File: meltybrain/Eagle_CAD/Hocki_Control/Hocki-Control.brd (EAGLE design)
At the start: 90 x 46 mm, 113 parts, among them J1 SM03B-SRSS-TB(LF)(SN), J2 SM03B-SRSS-TB(LF)(SN), U1 TEENSY_4.1, U10 TLV3502AIDCNR, U11 NL27WZ32USG, U12 NL27WZ32USG, U13 HMC1052L-TR, U14 LMV358, U15 IRF7509, U16 TMUX1219DCKR, U17 LMV358, U18 LMV358, U19 AP2210K-3.3TRG1, U2 ADXL375, U20 AP2210K-5.0TRG1, U21 MAX20075ATCA/V+, U3 ADXL375, U4 ADXL375, U5 ADXL375, U6 LMH6612MAX/NOPB, U7 LMH6612MAX/NOPB, U8 LMH6612MAX/NOPB, U9 LMH6612MAX/NOPB

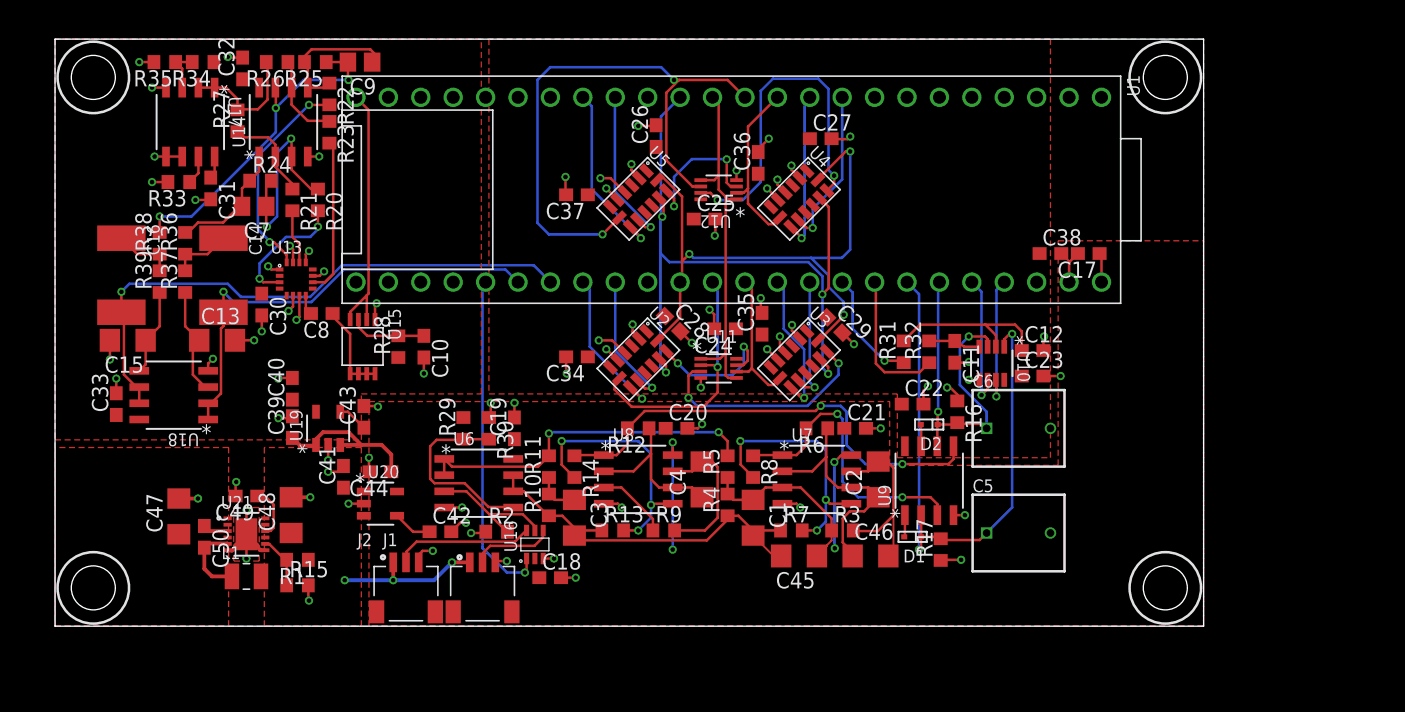
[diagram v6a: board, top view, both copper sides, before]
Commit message: errr---added a connector
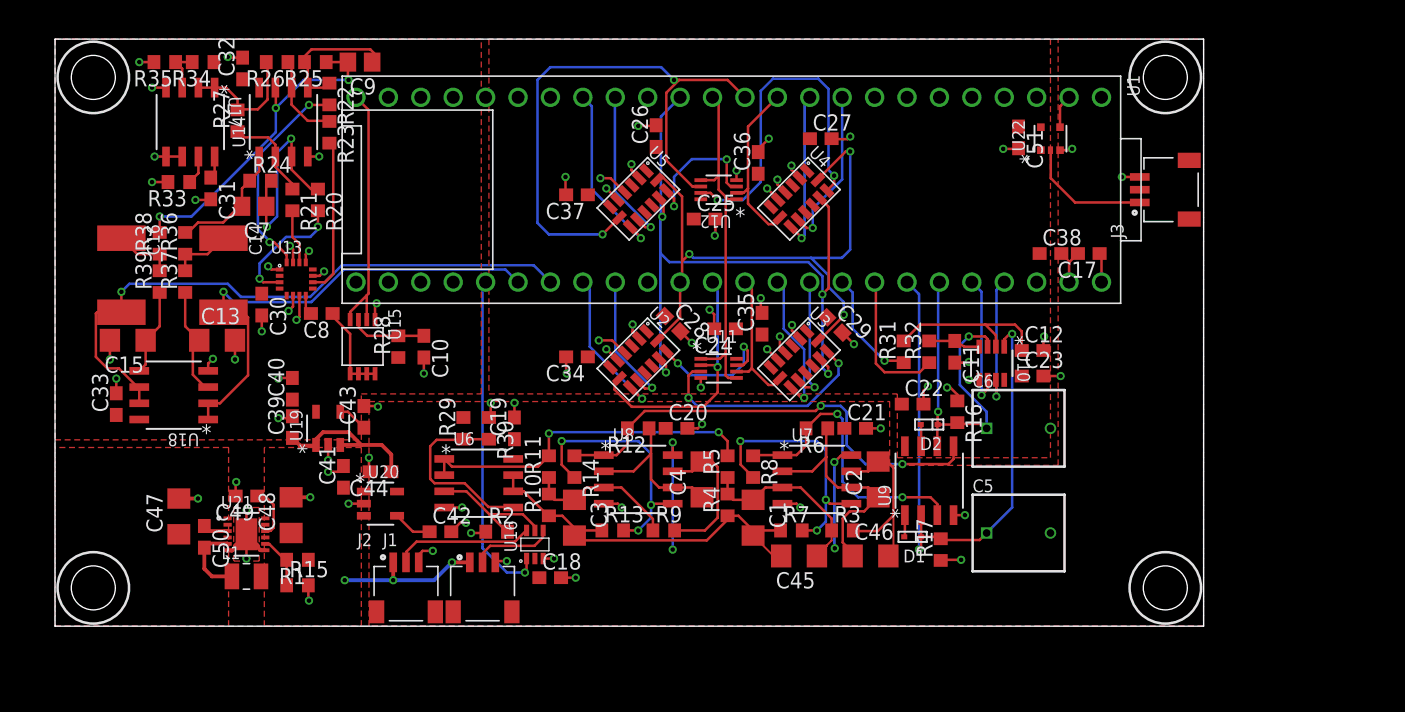
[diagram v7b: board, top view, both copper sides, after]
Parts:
- added C51: 0.1u, rcl:C0603
- added J3: SM03B-SRSS-TB(LF)(SN), Hocki_Library:SM03B-SRSS-TB(LF)(SN)
- added U22: 74AHC1G04GW,125, Hocki_Library:SOT-353
- R3, R6, R7, R8: value 160 -> 169
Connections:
- new net N$17: J3.1, U22.2
- new net SBUS: U1.0, U22.4
- net 3.3V: now also C51.1, U22.5
- net 5V: now also J3.2, J3.S1, J3.S2
- net GND: now also C51.2, J3.3, U22.3
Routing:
- net N$17: track 0.00 -> 9.97 mm
- net GND: track 112.2 -> 115.9 mm, vias 78 -> 81
- net MAG_FILT_B: track 45.3 -> 48.6 mm
- net MAG_FILT_A: track 35.5 -> 38.4 mm
- net SBUS: track 0.00 -> 2.63 mm
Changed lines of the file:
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@@
 <attribute name="VALUE" x="19.4" y="-5.6" size="1" layer="27" font="vector" rot="SR270" align="top-left"/>
 </element>
-<element name="R3" library="rcl" library_urn="urn:adsk.eagle:library:334" package="R0603" package3d_urn="urn:adsk.eagle:package:23555/3" value="160" x="9.7" y="-19.7" smashed="yes">
+<element name="R3" library="rcl" library_urn="urn:adsk.eagle:library:334" package="R0603" package3d_urn="urn:adsk.eagle:package:23555/3" value="169" x="9.7" y="-19.7" smashed="yes">
 <attribute name="NAME" x="9.065" y="-19.065" size="1.27" layer="25"/>
 <attribute name="POPULARITY" value="77" x="9.7" y="-19.7" size="1.778" layer="27" display="off"/>
@@
 <attribute name="VALUE" x="2.605" y="-15.335" size="1.27" layer="27" rot="R90"/>
 </element>
-<element name="R6" library="rcl" library_urn="urn:adsk.eagle:library:334" package="R0603" package3d_urn="urn:adsk.eagle:package:23555/3" value="160" x="7.7" y="-11.7" smashed="yes" rot="R180">
+<element name="R6" library="rcl" library_urn="urn:adsk.eagle:library:334" package="R0603" package3d_urn="urn:adsk.eagle:package:23555/3" value="169" x="7.7" y="-11.7" smashed="yes" rot="R180">
 <attribute name="NAME" x="8.335" y="-12.335" size="1.27" layer="25" rot="R180"/>
 <attribute name="POPULARITY" value="77" x="7.7" y="-11.7" size="1.778" layer="27" rot="R180" display="off"/>
@@
 <attribute name="VALUE" x="8.335" y="-9.795" size="1.27" layer="27" rot="R180"/>
 </element>
-<element name="R7" library="rcl" library_urn="urn:adsk.eagle:library:334" package="R0603" package3d_urn="urn:adsk.eagle:package:23555/3" value="160" x="5.7" y="-19.7" smashed="yes">
+<element name="R7" library="rcl" library_urn="urn:adsk.eagle:library:334" package="R0603" package3d_urn="urn:adsk.eagle:package:23555/3" value="169" x="5.7" y="-19.7" smashed="yes">
 <attribute name="NAME" x="5.065" y="-19.065" size="1.27" layer="25"/>
 <attribute name="POPULARITY" value="77" x="5.7" y="-19.7" size="1.778" layer="27" display="off"/>
@@
 <attribute name="VALUE" x="5.065" y="-21.605" size="1.27" layer="27"/>
 </element>
-<element name="R8" library="rcl" library_urn="urn:adsk.eagle:library:334" package="R0603" package3d_urn="urn:adsk.eagle:package:23555/3" value="160" x="2.7" y="-14.7" smashed="yes" rot="R270">
+<element name="R8" library="rcl" library_urn="urn:adsk.eagle:library:334" package="R0603" package3d_urn="urn:adsk.eagle:package:23555/3" value="169" x="2.7" y="-14.7" smashed="yes" rot="R270">
 <attribute name="NAME" x="3.335" y="-14.065" size="1.27" layer="25" rot="R270"/>
 <attribute name="POPULARITY" value="77" x="2.7" y="-14.7" size="1.778" layer="27" rot="R270" display="off"/>
@@
 <attribute name="SPICEPREFIX" value="R" x="-33" y="-24" size="1.778" layer="27" display="off"/>
 <attribute name="VALUE" x="-33.635" y="-25.905" size="1.27" layer="27"/>
+</element>
+<element name="J3" library="Hocki_Library" package="SM03B-SRSS-TB(LF)(SN)" value="SM03B-SRSS-TB(LF)(SN)" x="33" y="7" smashed="yes" rot="R90">
+<attribute name="DKPN" value="455-1803-1-ND" x="33" y="7" size="1.778" layer="27" rot="R90" display="off"/>
+<attribute name="NAME" x="31.73" y="3.19" size="1" layer="25" font="vector" rot="R90"/>
+<attribute name="VALUE" x="38.35" y="3.19" size="1" layer="27" font="vector" rot="R90" align="top-left"/>
+</element>
+<element name="U22" library="Hocki_Library" package="SOT-353" value="74AHC1G04GW,125" x="26" y="11" smashed="yes" rot="R90">
+<attribute name="DKPN" value="1727-3147-1-ND" x="26" y="11" size="1.778" layer="27" rot="R90" display="off"/>
+<attribute name="NAME" x="24" y="10" size="1" layer="25" font="vector" rot="SR90"/>
+<attribute name="VALUE" x="28" y="10" size="1" layer="27" font="vector" rot="SR90" align="top-left"/>
+</element>
+<element name="C51" library="rcl" library_urn="urn:adsk.eagle:library:334" package="C0603" package3d_urn="urn:adsk.eagle:package:23616/2" value="0.1u" x="23.5" y="11.1" smashed="yes" rot="R270">
+<attribute name="NAME" x="24.135" y="11.735" size="1.27" layer="25" rot="R270"/>
+<attribute name="POPULARITY" value="37" x="23.5" y="11.1" size="1.778" layer="27" rot="R270" display="off"/>
+<attribute name="SPICEPREFIX" value="C" x="23.5" y="11.1" size="1.778" layer="27" rot="R270" display="off"/>
+<attribute name="VALUE" x="21.595" y="11.735" size="1.27" layer="27" rot="R270"/>
 </element>
 </elements>
@@
 <wire x1="-47.7" y1="-4.8" x2="-47.7" y2="-6.3" width="0.2" layer="1"/>
 <via x="-47.7" y="-6.3" extent="1-16" drill="0.35"/>
-<wire x1="-37.9" y1="-4.8" x2="-36.4" y2="-4.8" width="0.2" layer="1"/>
-<via x="-36.4" y="-4.8" extent="1-16" drill="0.35"/>
+<wire x1="-37.9" y1="-4.8" x2="-37.9" y2="-6.3" width="0.2" layer="1"/>
+<via x="-37.9" y="-6.3" extent="1-16" drill="0.35"/>
 <wire x1="-47.2" y1="-7.8" x2="-47.2" y2="-8.95" width="0.2" layer="1"/>
 <via x="-47.2" y="-7.8" extent="1-16" drill="0.35"/>
@@
 <wire x1="-37" y1="-20" x2="-37" y2="-21.9" width="0.2" layer="1"/>
 <via x="-37" y="-21.9" extent="1-16" drill="0.35"/>
+<contactref element="J3" pad="3"/>
+<contactref element="U22" pad="3"/>
+<wire x1="26.75" y1="10.1" x2="27.7" y2="10.1" width="0.2" layer="1"/>
+<wire x1="27.7" y1="10.1" x2="27.7" y2="10.2" width="0.2" layer="1"/>
+<via x="27.7" y="10.2" extent="1-16" drill="0.35"/>
+<wire x1="33" y1="8" x2="31.6" y2="8" width="0.2" layer="1"/>
+<via x="31.6" y="8" extent="1-16" drill="0.35"/>
+<contactref element="C51" pad="2"/>
+<wire x1="23.5" y1="10.25" x2="23.45" y2="10.2" width="0.2" layer="1"/>
+<wire x1="23.45" y1="10.2" x2="22.3" y2="10.2" width="0.2" layer="1"/>
+<via x="22.3" y="10.2" extent="1-16" drill="0.35"/>
 </signal>
 <signal name="3.3V">
@@
 <contactref element="U1" pad="3.3V2"/>
 <contactref element="C38" pad="1"/>
+<contactref element="U22" pad="5"/>
+<contactref element="C51" pad="1"/>
 </signal>
 <signal name="MOSI">
@@
 <vertex x="13.4" y="-14.6"/>
 <vertex x="26.6" y="-14.6"/>
-<vertex x="26.6" y="3"/>
-<vertex x="38" y="3"/>
+<vertex x="26.6" y="18.8"/>
+<vertex x="38" y="18.8"/>
 <vertex x="38" y="-27.2"/>
 </polygon>
@@
 <wire x1="-25.65" y1="-13.75" x2="-26.4" y2="-13" width="0.3" layer="1"/>
 <wire x1="-26.4" y1="-13" x2="-28" y2="-13" width="0.3" layer="1"/>
+<contactref element="J3" pad="2"/>
+<contactref element="J3" pad="S2"/>
+<contactref element="J3" pad="S1"/>
 </signal>
 <signal name="VG_SIGNAL_BUF">
@@
 <wire x1="-38.8" y1="-1" x2="-38.8" y2="-2.6" width="0.2" layer="1"/>
 <wire x1="-40" y1="-11.005" x2="-40" y2="-9.735" width="0.2" layer="1"/>
-<wire x1="-38.8" y1="-2.6" x2="-38.8" y2="-3.678975" width="0.2" layer="1"/>
-<wire x1="-38.998" y1="-8.959025" x2="-39.773975" y2="-9.735" width="0.2" layer="1"/>
-<wire x1="-39.773975" y1="-9.735" x2="-40" y2="-9.735" width="0.2" layer="1"/>
-<wire x1="-38.8" y1="-3.678975" x2="-38.998" y2="-3.876975" width="0.2" layer="1"/>
-<wire x1="-38.998" y1="-3.876975" x2="-38.998" y2="-8.959025" width="0.2" layer="1"/>
+<wire x1="-36.873" y1="-3.005975" x2="-37.278975" y2="-2.6" width="0.2" layer="1"/>
+<wire x1="-38.8" y1="-2.6" x2="-37.278975" y2="-2.6" width="0.2" layer="1"/>
+<wire x1="-36.873" y1="-7.534025" x2="-39.073975" y2="-9.735" width="0.2" layer="1"/>
+<wire x1="-39.073975" y1="-9.735" x2="-40" y2="-9.735" width="0.2" layer="1"/>
+<wire x1="-36.873" y1="-3.005975" x2="-36.873" y2="-7.534025" width="0.2" layer="1"/>
 </signal>
 <signal name="N$29">
@@
 <wire x1="-29.53219375" y1="1.076" x2="-32.01101875" y2="-1.402825" width="0.2" layer="16"/>
 <wire x1="-46.8" y1="-1" x2="-46.8" y2="-2.6" width="0.2" layer="1"/>
-<wire x1="-45.4" y1="-8.465" x2="-45.626025" y2="-8.465" width="0.2" layer="1"/>
-<wire x1="-45.626025" y1="-8.465" x2="-46.602" y2="-7.489025" width="0.2" layer="1"/>
-<wire x1="-46.602" y1="-2.776975" x2="-46.778975" y2="-2.6" width="0.2" layer="1"/>
-<wire x1="-46.8" y1="-2.6" x2="-46.778975" y2="-2.6" width="0.2" layer="1"/>
-<wire x1="-46.602" y1="-2.776975" x2="-46.602" y2="-7.489025" width="0.2" layer="1"/>
+<wire x1="-45.626025" y1="-8.465" x2="-45.4" y2="-8.465" width="0.2" layer="1"/>
 <wire x1="-45.4" y1="-8.465" x2="-45.4" y2="-9.735" width="0.2" layer="1"/>
+<wire x1="-46.8" y1="-2.6" x2="-48.7" y2="-2.6" width="0.2" layer="1"/>
+<wire x1="-48.7" y1="-2.6" x2="-48.8" y2="-2.7" width="0.2" layer="1"/>
+<wire x1="-48.8" y1="-2.7" x2="-48.8" y2="-6.1" width="0.2" layer="1"/>
+<wire x1="-48.8" y1="-6.1" x2="-47.9" y2="-7" width="0.2" layer="1"/>
+<wire x1="-47" y1="-7" x2="-45.626025" y2="-8.373975" width="0.2" layer="1"/>
+<wire x1="-45.626025" y1="-8.373975" x2="-45.626025" y2="-8.465" width="0.2" layer="1"/>
+<wire x1="-47.9" y1="-7" x2="-47" y2="-7" width="0.2" layer="1"/>
 </signal>
 <signal name="+3V3">
@@
 <wire x1="-33.85" y1="-24" x2="-33.85" y2="-22" width="0.2" layer="1"/>
 </signal>
+<signal name="N$17">
+<contactref element="J3" pad="1"/>
+<contactref element="U22" pad="2"/>
+<wire x1="26" y1="10.1" x2="26.023" y2="10.077" width="0.2" layer="1"/>
+<wire x1="26.023" y1="10.077" x2="26.023" y2="7.905975" width="0.2" layer="1"/>
+<wire x1="26.023" y1="7.905975" x2="27.928975" y2="6" width="0.2" layer="1"/>
+<wire x1="27.928975" y1="6" x2="33" y2="6" width="0.2" layer="1"/>
+</signal>
+<signal name="SBUS">
+<contactref element="U22" pad="4"/>
+<contactref element="U1" pad="0"/>
+<wire x1="26.75" y1="11.9" x2="26.75" y2="13.53" width="0.2" layer="1"/>
+<wire x1="26.75" y1="13.53" x2="27.46" y2="14.24" width="0.2" layer="1"/>
+</signal>
 </signals>

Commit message: finished routing control?
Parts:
- added C52: 22u, rcl:C1206
- added C53: 4.7u, rcl:C0603
- added C54: 1u, rcl:C0603
- added CN1: (no value), Hocki_Library:JST-PH-2-SMT-RA
- added J4, J5: SM04B-SRSS-TB(LF)(SN), Hocki_Library:SM04B-SRSS-TB(LF)(SN)
- added U23: LDL212PU50R, Hocki_Library:DFN6(3X3)
- C47: value 4.7u -> 10u
- C49: value 1u -> 100p
- L1: value 4.7u -> 10uH; device Hocki_Library:1007 -> Hocki_Library:LQH5BPN100M38L
- R1: value 324k -> 205k
- R15: value 40.2k -> 20k
- U21: value MAX20075ATCA/V+ -> AP63200; device Hocki_Library:12-TDFN -> Hocki_Library:SOT-23-6
- moved R1 8.99 mm to (-39.0, -15.3)
- moved R15 8.99 mm to (-39.0, -17.3)
- moved C47 5.81 mm to (-39.7, -23.8), turned to 0 degrees
- moved C50 5.81 mm to (-36.0, -16.3), turned to 0 degrees
- moved C48 5.30 mm to (-33.7, -23.8), turned to 180 degrees
- moved L1 5.03 mm to (-33.2, -20.0)
- moved C49 4.21 mm to (-39.0, -13.3)
- moved U21 1.20 mm to (-38.2, -20.0)
- moved C41 0.91 mm to (-30.3, -15.6)
- moved C44 0.91 mm to (-27.4, -15.2)
- moved U20 0.91 mm to (-27.4, -17.7)
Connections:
- removed net N$6: C49.1, U21.10
- new net +5V: C53.1, J4.1, J4.S1, J4.S2, J5.1, J5.S1, J5.S2, U23.2, U23.3
- new net LED_CLK1: J4.2, U1.2
- new net LED_CLK2: J5.2, U1.4
- new net LED_DATA1: J4.3, U1.1
- new net LED_DATA2: J5.3, U1.3
- net +24V: now also CN1.1, CN1.NC1, CN1.NC2, U21.3; no longer U21.4
- net 9V: now also C49.1, C52.1, C54.1, U23.4; no longer U21.9
- net GND: now also C52.2, C53.2, C54.2, CN1.2, J4.4, J5.4, U21.4, U23.1, U23.7; no longer C49.2, U21.13, U21.6, U21.7
- net N$1: now also U21.6; no longer U21.3
- net N$12: now also C49.2, U21.1; no longer U21.8
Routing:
- net 9V: track 11.8 -> 89.8 mm, vias 3 -> 5
- net LED_CLK2: track 0.00 -> 30.8 mm, vias 0 -> 1
- net LED_DATA2: track 0.00 -> 27.9 mm, vias 0 -> 1
- net LED_CLK1: track 0.00 -> 21.6 mm, vias 0 -> 1
- net LED_DATA1: track 0.00 -> 18.8 mm, vias 0 -> 1
- net N$3: track 6.03 -> 0.00 mm
- net N$6: track 4.13 -> 0.00 mm
- net GND: track 115.9 -> 112.1 mm, vias 81 -> 89
- net N$12: track 4.19 -> 6.00 mm
- net IR_SEL: track 26.2 -> 25.2 mm
- net N$1: track 1.99 -> 2.85 mm
- net 5V: track 32.5 -> 31.6 mm
- net N$8: track 3.07 -> 3.93 mm
- added copper zone on layer 1, net +5V
- added copper zone on layer 1, net N$3
